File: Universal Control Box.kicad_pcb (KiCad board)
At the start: 4 copper layers, 168.2 x 98.8 mm, 88 parts, among them J101 Conn_01x06, J102 Conn_01x07, J103 USB_C_Receptacle_USB2.0, U101 ESP32-WROOM-32, U102 PCF8575DBR (PCF1), U103 XC6220B331MR-G, U201 PEC11H-4025F-S0016, U202 PEC11H-4025F-S0016

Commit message: update design
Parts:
- added REF**: KiCad-Logo2_8mm_SilkScreen, Symbol:KiCad-Logo2_8mm_SilkScreen, F.Cu at (137.6, 32.3)
- added U104: 74AHCT1G125, Package_TO_SOT_SMD:SOT-23-5, F.Cu at (40.1, 57.3)
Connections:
- SW301 pad 5: /LED_DATA -> /LED_DATA_OUT
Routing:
- net /LED_DATA_OUT: track 0.00 -> 30.2 mm
- net /LED_DATA: track 47.4 -> 18.2 mm
- net +5V: track 183.0 -> 190.8 mm, vias 46 -> 47
- net GND: track 132.7 -> 135.0 mm, vias 59 -> 61
- net /IO_INT: track 51.4 -> 52.8 mm
- net /Rotary Encoders/SW_RSW2: track 146.0 -> 144.7 mm
- net /I2C_SCL: track 72.6 -> 73.6 mm
- net /Rotary Encoders/SW_RSW1: track 96.1 -> 95.2 mm
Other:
- board text added: "Fix spacing between signal lines (MOSI and SCK)"
- board text added: "Fix traces"
- board text added: "Pick different GPIO pins for CS/DC/Reset"

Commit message: Fixes
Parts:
- removed the REF** at (137.6, 32.3)
- added REF**: KiCad-Logo2_6mm_SilkScreen, Symbol:KiCad-Logo2_6mm_SilkScreen, F.Cu at (137.7, 28.9)
- added REF**: OSHW-Logo2_9.8x8mm_SilkScreen, Symbol:OSHW-Logo2_9.8x8mm_SilkScreen, F.Cu at (172.1, 31.2)
- moved U104 7.42 mm to (35.7, 51.4)
- moved C201 1.50 mm to (114.1, 60.1)
- moved C202 1.50 mm to (122.3, 60.1)
- moved R201 1.50 mm to (115.7, 60.1)
- moved R202 1.50 mm to (111.7, 57.7)
- moved R203 1.50 mm to (124.7, 57.7)
- moved R204 1.50 mm to (120.7, 60.1)
- moved R206 1.50 mm to (150.2, 57.7)
- moved R207 1.50 mm to (163.2, 57.7)
- moved U201 1.50 mm to (118.2, 47.8)
- moved U202 1.50 mm to (156.7, 47.8)
- moved C203 1.40 mm to (152.6, 60.1)
- moved C204 1.40 mm to (160.8, 60.1)
- moved R205 1.40 mm to (154.2, 60.1)
- moved R208 1.40 mm to (159.2, 60.1)
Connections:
- U101 pad 29: /OLED_CS -> unconnected-(U101-IO5-Pad29)
- U101 pad 6: unconnected-(U101-IO34-Pad6) -> /OLED_CS
- U101 pad 7: unconnected-(U101-IO35-Pad7) -> /OLED_DC
- U101 pad 9: /OLED_DC -> unconnected-(U101-IO33-Pad9)
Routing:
- net /OLED_CS: track 38.8 -> 22.3 mm, vias 2 -> 0
- net +5V: track 190.8 -> 201.2 mm, vias 47 -> 42
- net /LED_DATA: track 18.2 -> 10.6 mm
- net Net-(SW308-DOUT): track 174.9 -> 169.7 mm
- net /LED_DATA_OUT: track 30.2 -> 32.8 mm
- net /Rotary Encoders/A_RSW2: track 110.3 -> 108.8 mm
- net Net-(U202-CHANNEL_2): track 7.88 -> 9.21 mm
- net Net-(U202-CHANNEL_1): track 7.88 -> 9.21 mm
- net Net-(U201-CHANNEL_2): track 7.98 -> 9.21 mm
- net Net-(U201-CHANNEL_1): track 7.98 -> 9.21 mm
- net /Rotary Encoders/A_RSW1: track 70.9 -> 69.7 mm
- net GND: track 135.0 -> 136.0 mm, vias 61 -> 57
- net /OLED_MOSI: track 44.3 -> 45.3 mm
- net /OLED_SCL: track 38.1 -> 39.0 mm
- net /OLED_RESET: track 20.9 -> 20.3 mm
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- removed copper zone on F.Cu, net +5V
- removed copper zone on In1.Cu, net +5V
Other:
- board text added: "Universal Control Box ${REVISION}"
- board text removed: "Fix spacing between signal lines (MOSI and SCK)"
- board text removed: "Fix traces"
- board text removed: "Pick different GPIO pins for CS/DC/Reset"
- board text removed: "Universal Controller ${REVISION}"

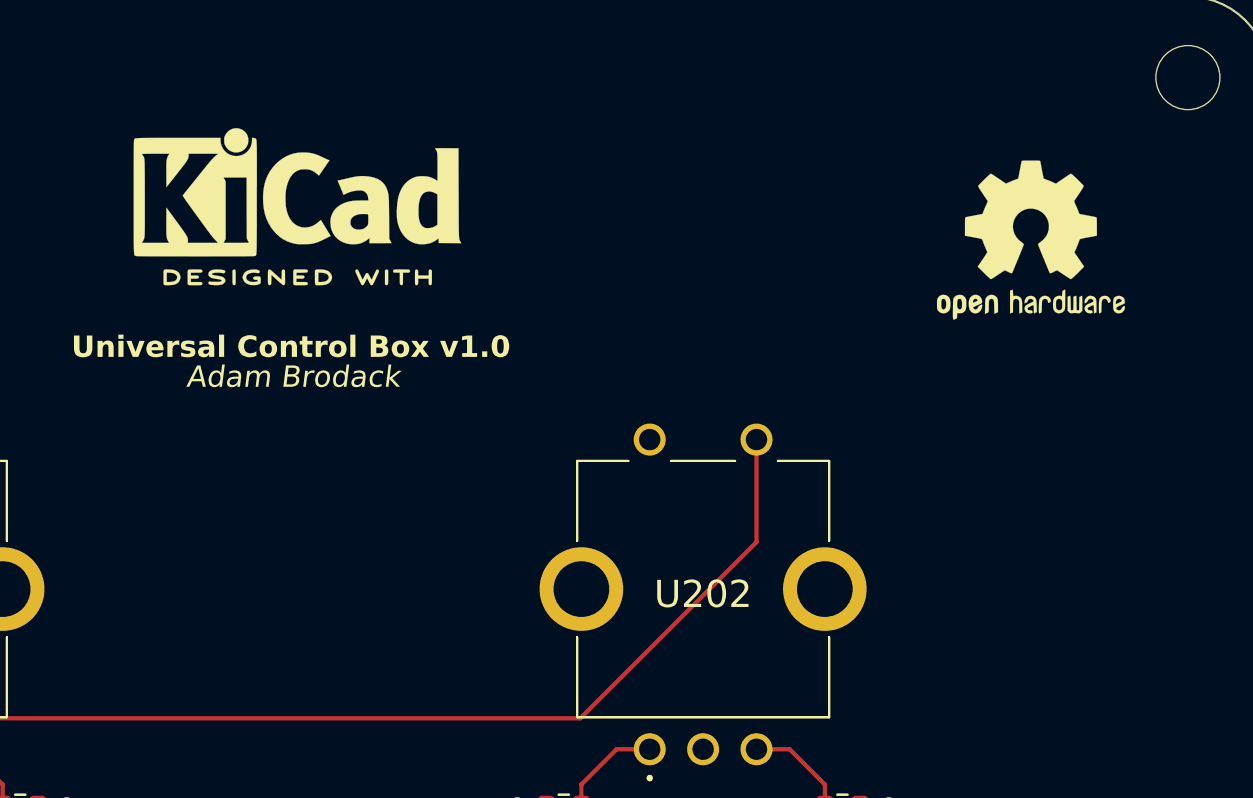
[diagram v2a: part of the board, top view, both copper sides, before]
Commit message: Updated keycap & added missing logos
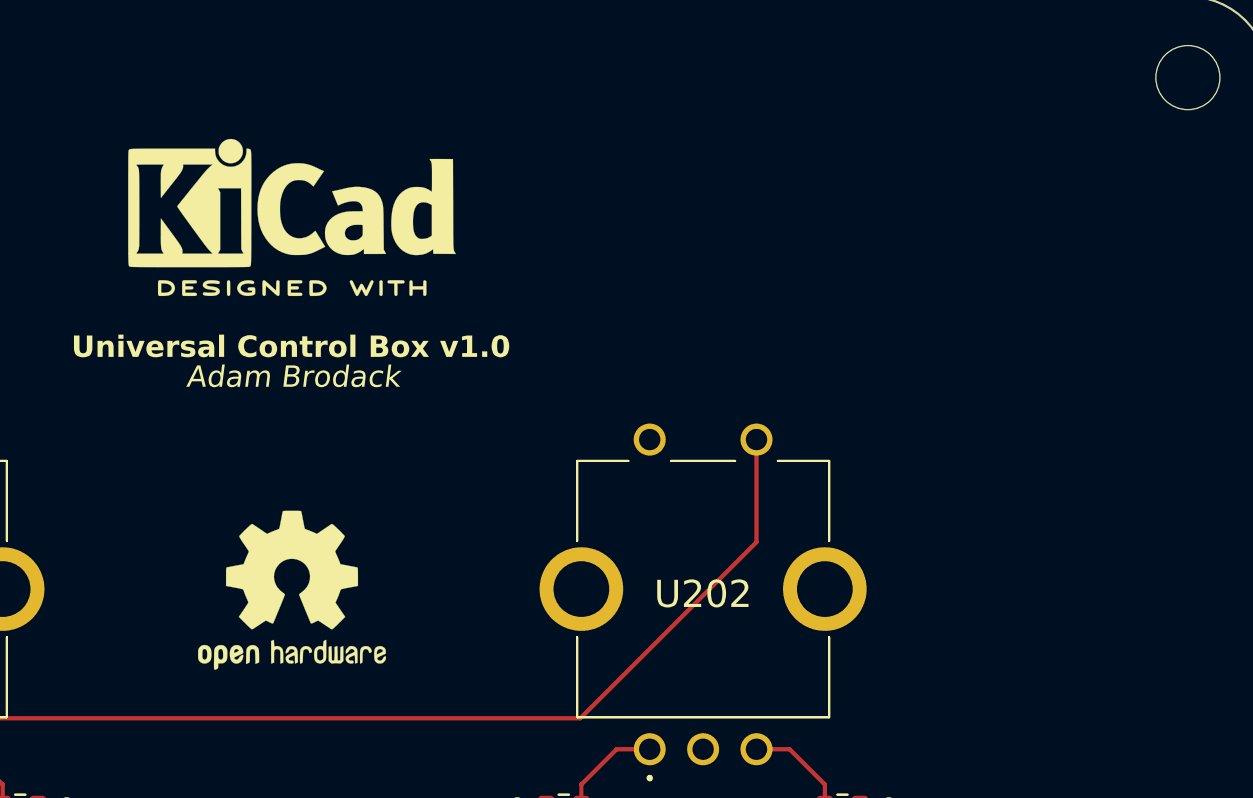
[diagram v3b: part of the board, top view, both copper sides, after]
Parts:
- moved REF** 38.3 mm to (137.4, 47.6)
- moved REF** 0.57 mm to (137.4, 29.5)
